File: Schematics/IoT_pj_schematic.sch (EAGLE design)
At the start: 109 parts, among them J1 -, J6 -, J7 -, Q1 2N7002, Q2 SIA817, Q3 2N7002, Q5 2N7002DW-7-FNO_PAD, U1 D21G18, U2 SN74AVC4T774, U3 SARA-U201, U5 BQ24195L, U6 AP721533, U7 SN74AVC4T774, Y1 32768Hz

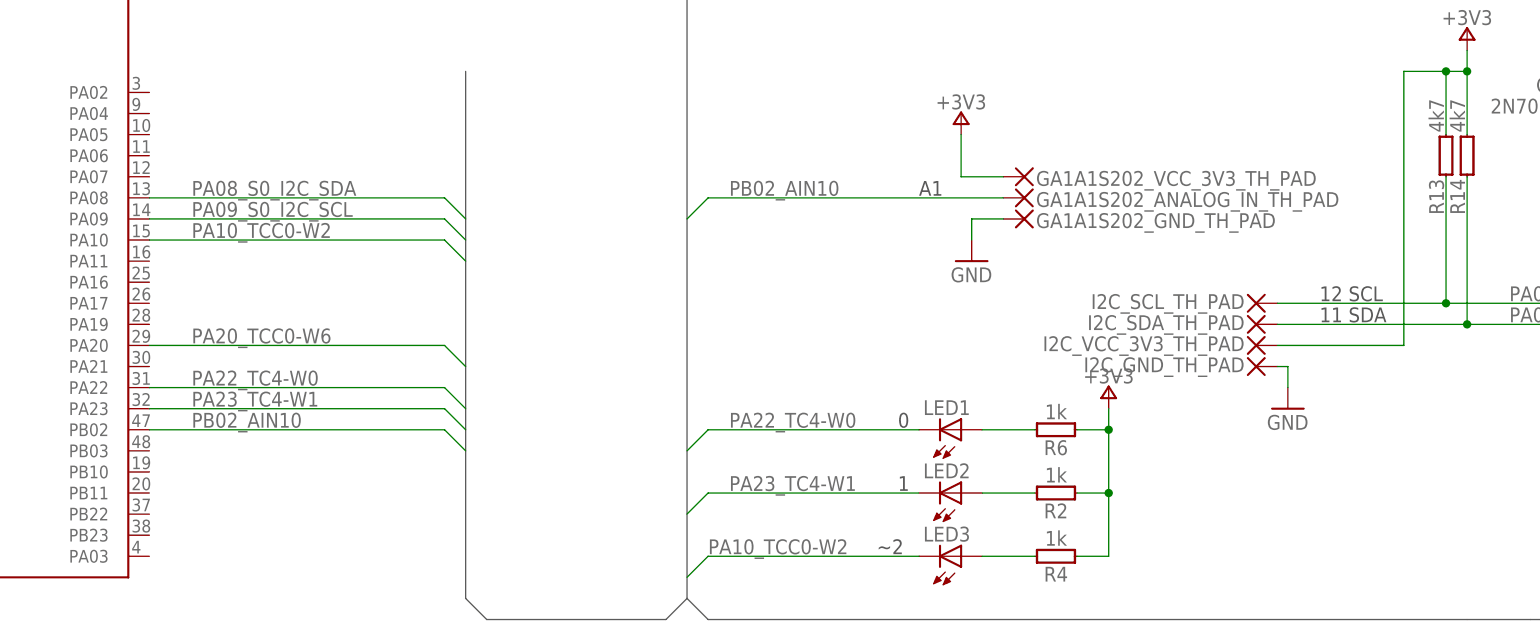
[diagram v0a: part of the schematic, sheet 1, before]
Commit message: FIx: Silkscreen names and values corrected
Corrected the position so they wouldn't overlap
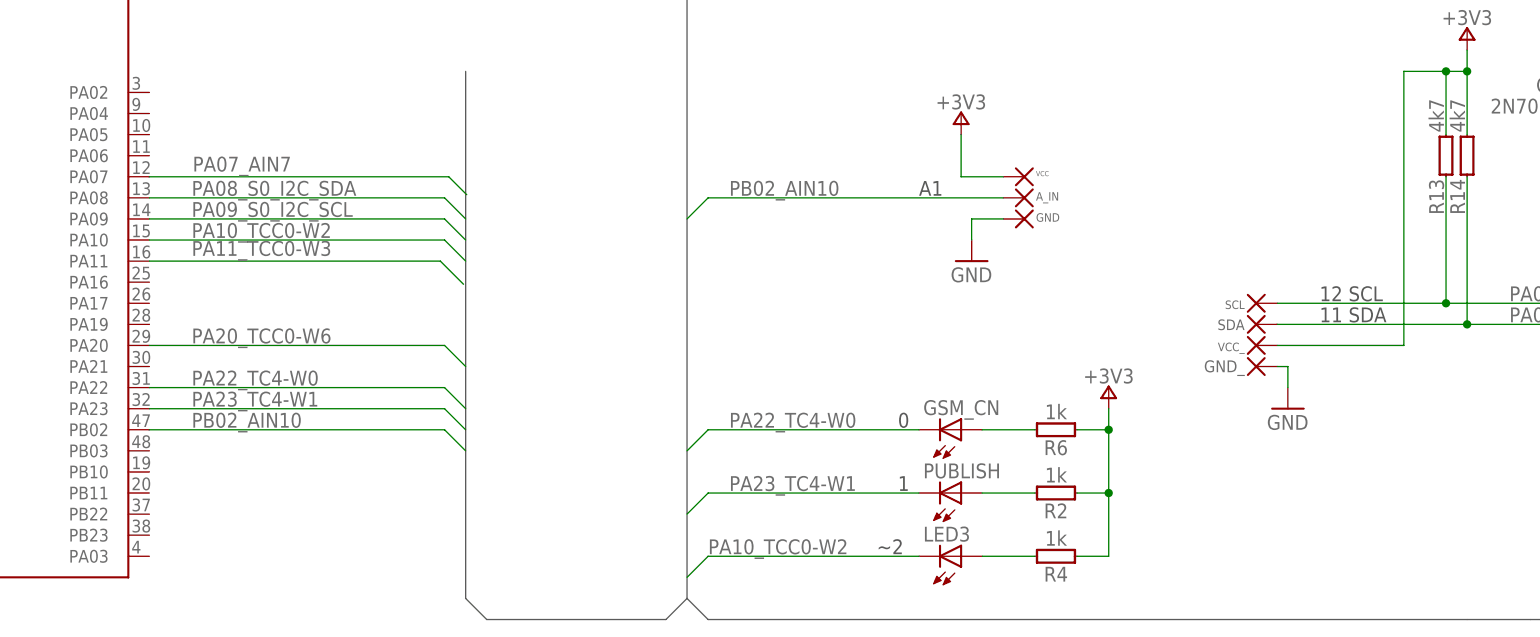
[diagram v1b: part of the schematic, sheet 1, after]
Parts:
- renumbered GA1A1S202_ANALOG_IN_TH_PAD to A_IN, GA1A1S202_GND_TH_PAD to GND, GA1A1S202_VCC_3V3_TH_PAD to VCC, I2C_GND_TH_PAD to GND_, I2C_SCL_TH_PAD to SCL, I2C_SDA_TH_PAD to SDA, I2C_VCC_3V3_TH_PAD to VCC_, LED1 to GSM_CN, LED2 to PUBLISH
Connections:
- net PA07_AIN7: now also U1A.PA07
- net PA11_TCC0-W3: now also U1A.PA11

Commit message: Fix: LED 3 name to MQTT_Conn
Add: Shielding vias
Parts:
- renumbered LED3 to MQTT_CON
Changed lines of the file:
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@@
 <part name="GSM_CN" library="led" library_urn="urn:adsk.eagle:library:259" deviceset="LED" device="SML0603" package3d_urn="urn:adsk.eagle:package:15832/1"/>
 <part name="PUBLISH" library="led" library_urn="urn:adsk.eagle:library:259" deviceset="LED" device="SML0603" package3d_urn="urn:adsk.eagle:package:15832/1"/>
-<part name="LED3" library="led" library_urn="urn:adsk.eagle:library:259" deviceset="LED" device="SML0603" package3d_urn="urn:adsk.eagle:package:15832/1"/>
+<part name="MQTT_CON" library="led" library_urn="urn:adsk.eagle:library:259" deviceset="LED" device="SML0603" package3d_urn="urn:adsk.eagle:package:15832/1"/>
 <part name="R2" library="Arduino-rcl" deviceset="R" device="-0402" technology="-1K" value="1k"/>
 <part name="R4" library="Arduino-rcl" deviceset="R" device="-0402" technology="-1K" value="1k"/>
@@
 <attribute name="VALUE" x="241.808" y="46.355" size="1.778" layer="96" rot="MR180"/>
 </instance>
-<instance part="LED3" gate="G$1" x="246.38" y="33.02" smashed="yes" rot="MR90">
+<instance part="MQTT_CON" gate="G$1" x="246.38" y="33.02" smashed="yes" rot="MR90">
 <attribute name="NAME" x="241.808" y="36.576" size="1.778" layer="95" rot="MR180"/>
 <attribute name="VALUE" x="241.808" y="38.735" size="1.778" layer="96" rot="MR180"/>
@@
 <label x="215.9" y="33.274" size="1.778" layer="95"/>
 <wire x1="213.36" y1="30.48" x2="215.9" y2="33.02" width="0.1524" layer="91"/>
-<pinref part="LED3" gate="G$1" pin="C"/>
+<pinref part="MQTT_CON" gate="G$1" pin="C"/>
 </segment>
 <segment>
@@
 <net name="N$25" class="0">
 <segment>
-<pinref part="LED3" gate="G$1" pin="A"/>
+<pinref part="MQTT_CON" gate="G$1" pin="A"/>
 <pinref part="R4" gate="G$1" pin="2"/>
 <wire x1="248.92" y1="33.02" x2="255.27" y2="33.02" width="0.1524" layer="91"/>
